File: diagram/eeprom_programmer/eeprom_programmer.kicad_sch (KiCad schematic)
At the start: 2 parts

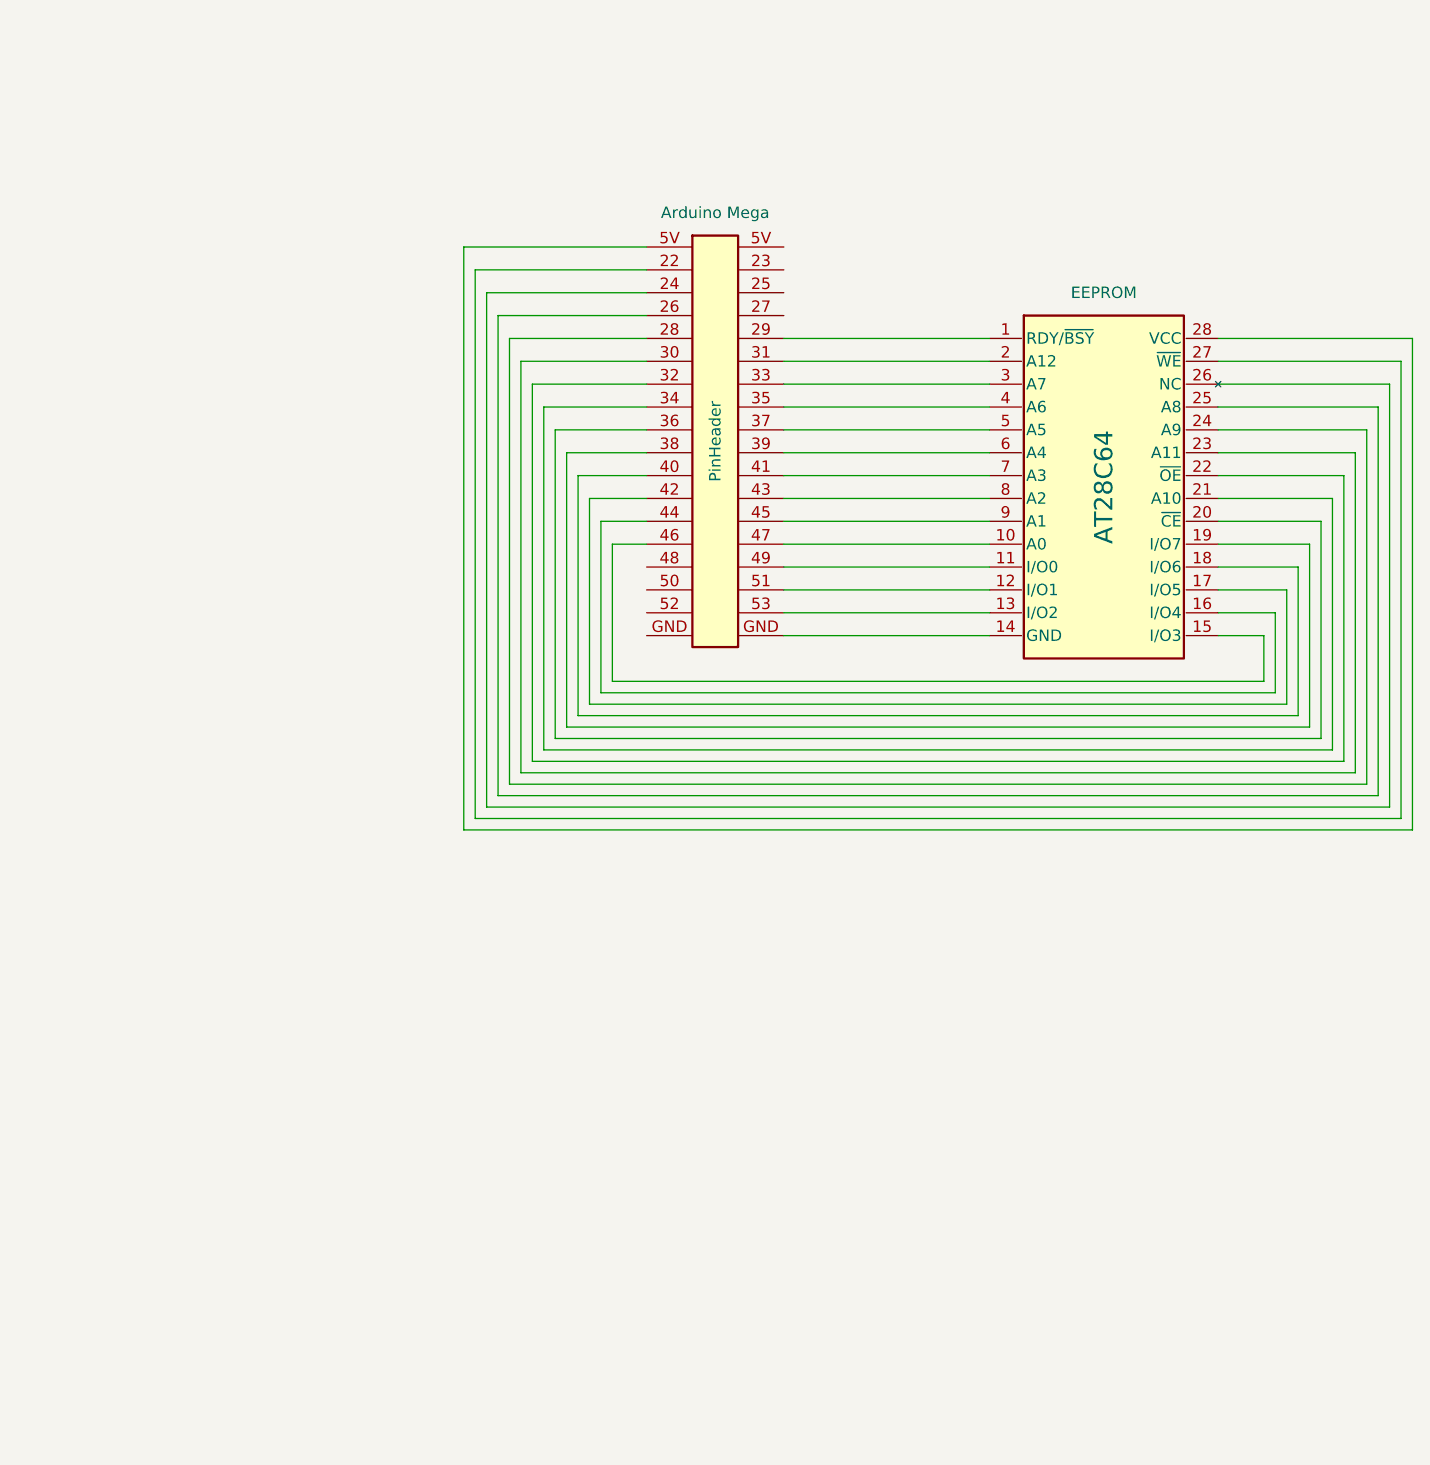
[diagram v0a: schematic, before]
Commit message: add wiring diagram for AT28C16
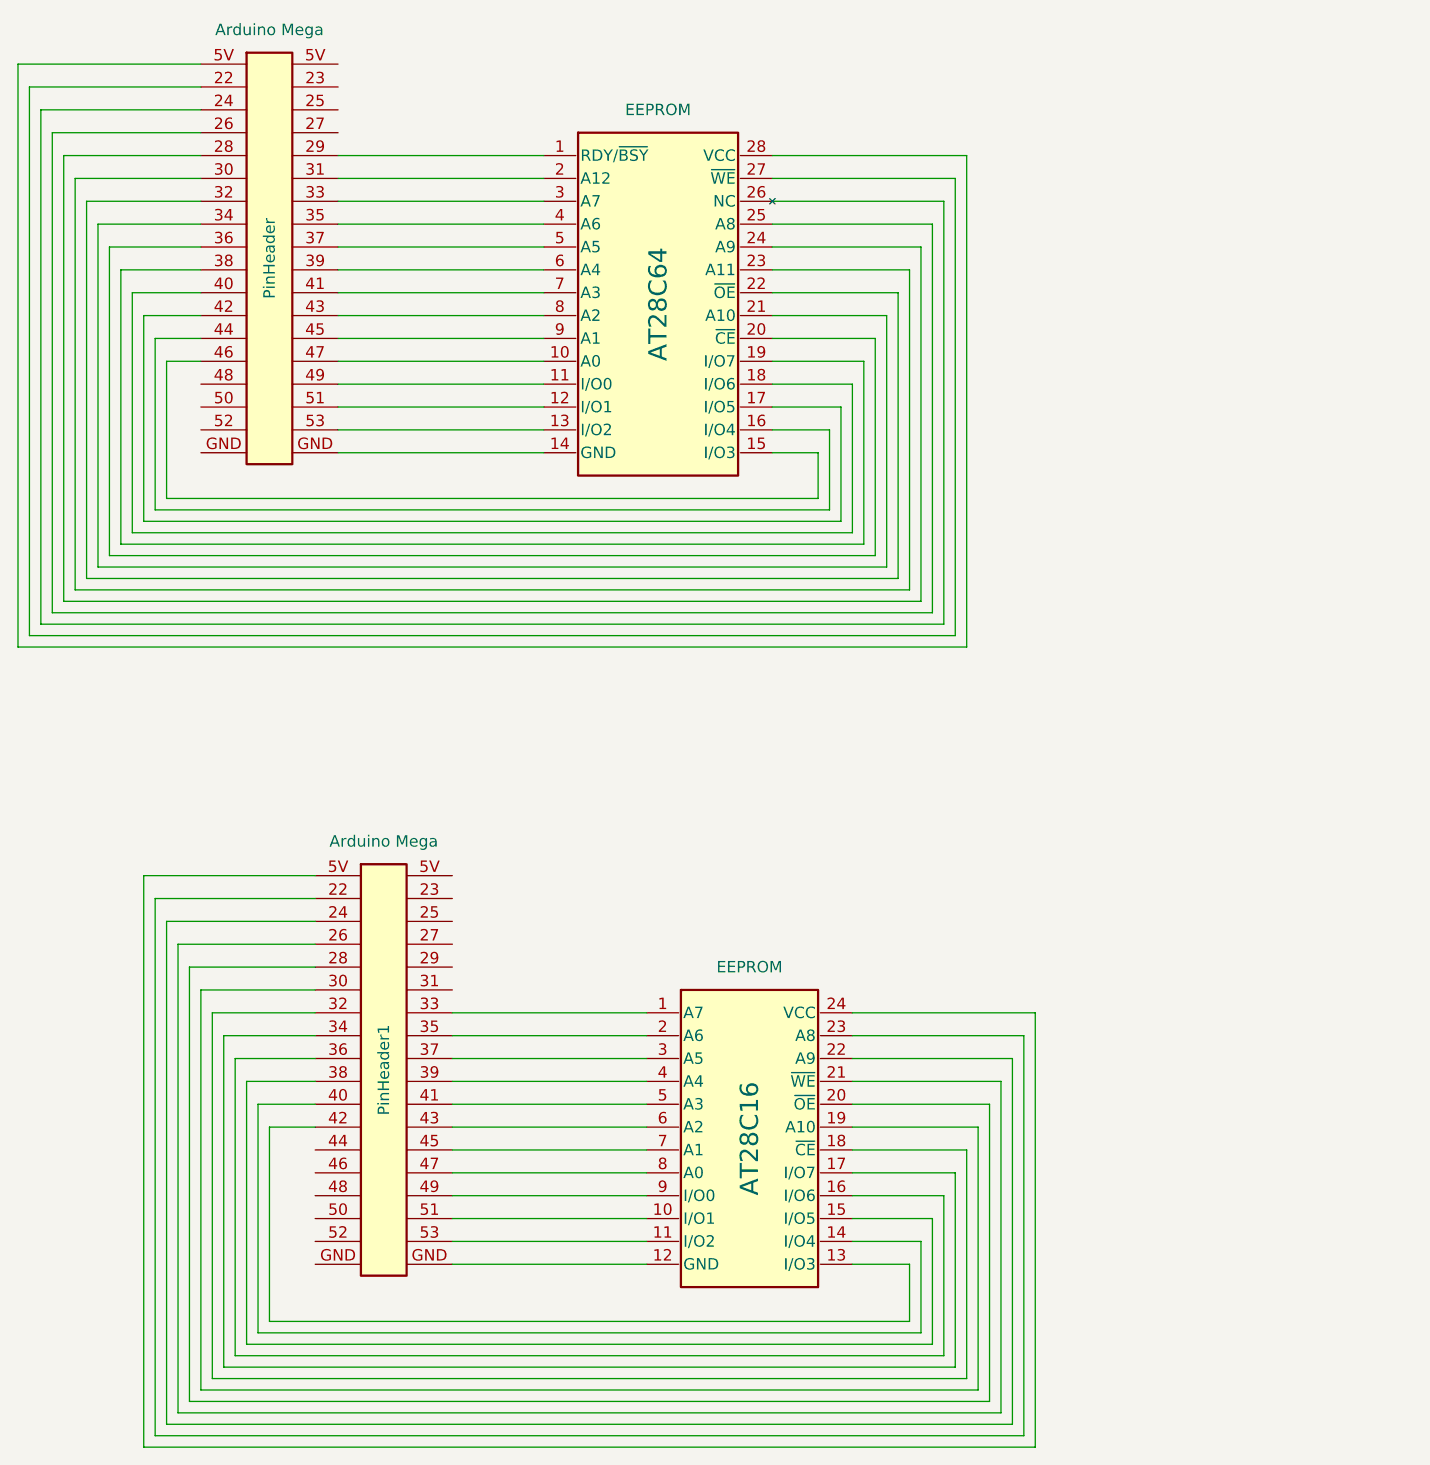
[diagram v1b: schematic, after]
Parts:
- added AT28C16: EEPROM, symbol inn_goose:AT28C16
- added PinHeader1: Arduino Mega, symbol MCU_Module:Arduino_Mega_2560_PinHeader
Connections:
- new net: AT28C16.23 (A8), PinHeader1.22
- new net: AT28C16.22 (A9), PinHeader1.24
- new net: AT28C16.21 (~{WE}), PinHeader1.26
- new net: AT28C16.20 (~{OE}), PinHeader1.28
- new net: AT28C16.19 (A10), PinHeader1.30
- new net: AT28C16.18 (~{CE}), PinHeader1.32
- new net: AT28C16.1 (A7), PinHeader1.33
- new net: AT28C16.17 (I/O7), PinHeader1.34
- new net: AT28C16.2 (A6), PinHeader1.35
- new net: AT28C16.16 (I/O6), PinHeader1.36
- new net: AT28C16.3 (A5), PinHeader1.37
- new net: AT28C16.15 (I/O5), PinHeader1.38
- new net: AT28C16.4 (A4), PinHeader1.39
- new net: AT28C16.14 (I/O4), PinHeader1.40
- new net: AT28C16.5 (A3), PinHeader1.41
- new net: AT28C16.13 (I/O3), PinHeader1.42
- new net: AT28C16.6 (A2), PinHeader1.43
- new net: AT28C16.7 (A1), PinHeader1.45
- new net: AT28C16.8 (A0), PinHeader1.47
- new net: AT28C16.9 (I/O0), PinHeader1.49
- new net: AT28C16.10 (I/O1), PinHeader1.51
- new net: AT28C16.11 (I/O2), PinHeader1.53
- new net: AT28C16.24 (VCC), PinHeader1.5V
- new net: AT28C16.12 (GND), PinHeader1.GND
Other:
- moved on the sheet: AT28C64, PinHeader

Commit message: add comments; fix wiring diagrams
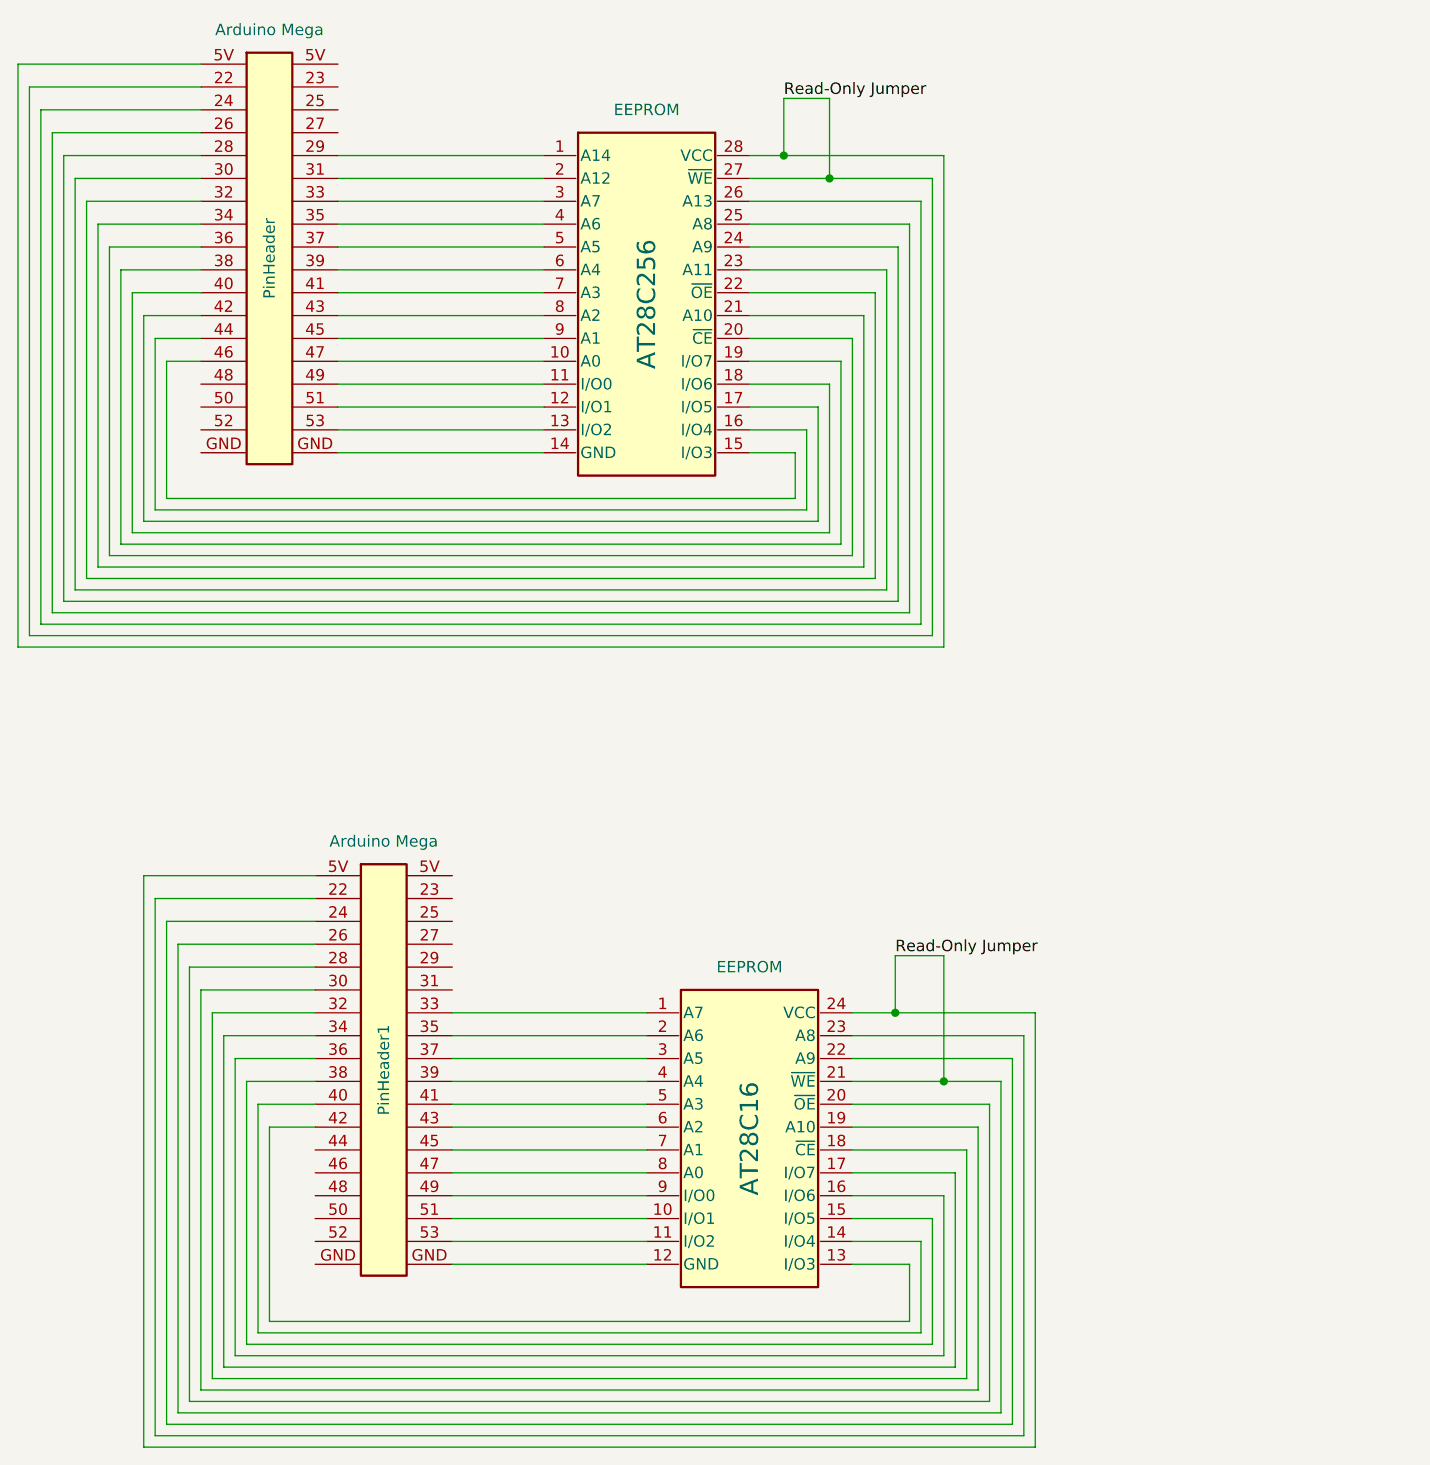
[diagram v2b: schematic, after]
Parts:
- removed AT28C64: EEPROM, symbol Memory_EEPROM:AT28C64
- added AT28C256: EEPROM, symbol inn_goose:AT28C256
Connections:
- net Read-Only Jumper: now reaches AT28C16.21 (~{WE}), PinHeader1.26
- net Read-Only Jumper: now also AT28C16.24 (VCC), PinHeader.22, PinHeader.5V, PinHeader1.5V, AT28C256.27 (~{WE}), AT28C256.28 (VCC)
- net at PinHeader1.GND: now also AT28C16.12 (GND)
- net at PinHeader.29: now also AT28C256.1 (A14)
- net at PinHeader.47: now also AT28C256.10 (A0)
- net at PinHeader.49: now also AT28C256.11 (I/O0)
- net at PinHeader.51: now also AT28C256.12 (I/O1)
- net at PinHeader.53: now also AT28C256.13 (I/O2)
- net at PinHeader.46: now also AT28C256.15 (I/O3)
- net at PinHeader.44: now also AT28C256.16 (I/O4)
- net at PinHeader.42: now also AT28C256.17 (I/O5)
- net at PinHeader.40: now also AT28C256.18 (I/O6)
- net at PinHeader.38: now also AT28C256.19 (I/O7)
- net at PinHeader.31: now also AT28C256.2 (A12)
- net at PinHeader.36: now also AT28C256.20 (~{CE})
- net at PinHeader.34: now also AT28C256.21 (A10)
- net at PinHeader.32: now also AT28C256.22 (~{OE})
- net at PinHeader.30: now also AT28C256.23 (A11)
- net at PinHeader.28: now also AT28C256.24 (A9)
- net at PinHeader.26: now also AT28C256.25 (A8)
- net at PinHeader.24: now also AT28C256.26 (A13)
- net at PinHeader.33: now also AT28C256.3 (A7)
- net at PinHeader.35: now also AT28C256.4 (A6)
- net at PinHeader.37: now also AT28C256.5 (A5)
- net at PinHeader.39: now also AT28C256.6 (A4)
- net at PinHeader.41: now also AT28C256.7 (A3)
- net at PinHeader.43: now also AT28C256.8 (A2)
- net at PinHeader.45: now also AT28C256.9 (A1)
- new net: AT28C256.14 (GND), PinHeader.GND
